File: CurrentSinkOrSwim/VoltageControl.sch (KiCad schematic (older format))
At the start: 7 parts, among them U201 LMV358

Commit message: cambiando potenciómetro y divisores de tension
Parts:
- R201: value R -> 27,8K
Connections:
- net 2.7V: now also R201.1; no longer RV201.2
- net Current_Sink-: now also RV201.3; no longer R201.2
- new net: R201.2, RV201.2, U201.3 (+)
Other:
- note added: "0-20V"
- note added: "0-2V"
- note added: "Como queremos que como máximo tengamos 20V (porque con 1A de mínimo\nen la fuente de corriente, con 20V de batería en el MOSFET se disipan 20W), el\ndivisor de tensión tendrá que dar en el + 2V."
- note added: "Con este potenciómetro controlar el máximo voltaje de la batería.\nEl valor que pongas en el + lo multiplicas por 10 y ese es el valor máximo"
- note added: "Si la batería supera los 20V, el MOSFET tendrá que dejar de funcionar y la batería se conecta directamente a tierra"
- moved on the sheet: R201
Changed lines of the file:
@@
 Sheet 2 4
 Title ""
-Date "7 sep 2015"
+Date "19 sep 2015"
 Rev ""
 Comp ""
@@
 L R R201
 U 1 1 55E5F049
-P 3600 5200
-F 0 "R201" V 3680 5200 40  0000 C CNN
-F 1 "R" V 3607 5201 40  0000 C CNN
-F 2 "~" V 3530 5200 30  0000 C CNN
-F 3 "~" H 3600 5200 30  0000 C CNN
-	1    3600 5200
+P 3900 3650
+F 0 "R201" V 3980 3650 40  0000 C CNN
+F 1 "27,8K" V 3907 3651 40  0000 C CNN
+F 2 "~" V 3830 3650 30  0000 C CNN
+F 3 "~" H 3900 3650 30  0000 C CNN
+	1    3900 3650
 	1    0    0    -1
 $EndComp
@@
 	5850 4100 5850 4250
 Wire Wire Line
-	3600 4600 3600 4950
-Wire Wire Line
 	5450 3800 5200 3800
 Wire Wire Line
@@
 	5450 3600 4800 3600
 Wire Wire Line
-	4800 3600 4800 4750
-Wire Wire Line
-	4800 4750 3600 4750
-Connection ~ 3600 4750
-Wire Wire Line
-	3600 5450 3600 5550
+	3600 4600 3600 5550
 Wire Wire Line
 	3600 5550 9200 5550
-Wire Wire Line
-	3900 4350 3750 4350
 Wire Wire Line
 	5850 2950 5850 3300
@@
 Wire Wire Line
 	3250 1900 3900 1900
-Wire Wire Line
-	3900 1900 3900 4350
-Connection ~ 3900 2950
 Wire Wire Line
 	6450 3700 6800 3700
@@
 Text HLabel 9200 3700 2    60   Output ~ 0
 Vcontrol
+Text Notes 750  1000 0    60   ~ 0
+Con este potenciómetro controlar el máximo voltaje de la batería.\nEl valor que pongas en el + lo multiplicas por 10 y ese es el valor máximo
+Text Notes 750  1200 0    60   ~ 0
+Como queremos que como máximo tengamos 20V (porque con 1A de mínimo\nen la fuente de corriente, con 20V de batería en el MOSFET se disipan 20W), el\ndivisor de tensión tendrá que dar en el + 2V.
+Text Notes 750  1500 0    60   ~ 0
+Si la batería supera los 20V, el MOSFET tendrá que dejar de funcionar y la batería se conecta directamente a tierra
+Wire Wire Line
+	3900 1900 3900 3400
+Wire Wire Line
+	3750 4350 4800 4350
+Wire Wire Line
+	3900 3900 3900 4350
+Connection ~ 3900 2950
+Wire Wire Line
+	4800 4350 4800 3600
+Connection ~ 3900 4350
+Text Notes 4250 4350 0    60   ~ 0
+0-2V
+Text Notes 6700 4450 0    60   ~ 0
+0-2V
+Text Notes 8800 3850 0    60   ~ 0
+0-20V
 $EndSCHEMATC

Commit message: placing components in the PCB
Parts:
- renumbered 1N4148WT-7 to D201
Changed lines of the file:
@@
 $EndComp
 $Comp
-L GND #PWR03
+L GND #PWR202
 U 1 1 55E5F04F
 P 5850 4250
-F 0 "#PWR03" H 5850 4250 30  0001 C CNN
+F 0 "#PWR202" H 5850 4250 30  0001 C CNN
 F 1 "GND" H 5850 4180 30  0001 C CNN
 F 2 "~" H 5850 4250 60  0000 C CNN
@@
 $EndComp
 $Comp
-L GND #PWR04
+L GND #PWR201
 U 1 1 55E5F061
 P 5350 3450
-F 0 "#PWR04" H 5350 3450 30  0001 C CNN
+F 0 "#PWR201" H 5350 3450 30  0001 C CNN
 F 1 "GND" H 5350 3380 30  0001 C CNN
 F 2 "~" H 5350 3450 60  0000 C CNN
@@
 	6450 3700 6800 3700
 $Comp
-L DIODE 1N4148WT-7
+L DIODE D201
 U 1 1 55E5F084
 P 7000 3700
-F 0 "1N4148WT-7" H 7000 3800 40  0000 C CNN
+F 0 "D201" H 7000 3800 40  0000 C CNN
 F 1 "DIODE" H 7000 3600 40  0000 C CNN
 F 2 "~" H 7000 3700 60  0000 C CNN

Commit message: Layout session 2
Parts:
- removed C201: C, ~, symbol C
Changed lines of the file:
@@
 Sheet 2 4
 Title ""
-Date "19 sep 2015"
+Date "24 sep 2015"
 Rev ""
 Comp ""
@@
 $EndComp
 $Comp
-L GND #PWR202
+L GND #PWR03
 U 1 1 55E5F04F
 P 5850 4250
-F 0 "#PWR202" H 5850 4250 30  0001 C CNN
+F 0 "#PWR03" H 5850 4250 30  0001 C CNN
 F 1 "GND" H 5850 4180 30  0001 C CNN
 F 2 "~" H 5850 4250 60  0000 C CNN
@@
 	1    3600 4350
 	0    1    1    0
-$EndComp
-$Comp
-L C C201
-U 1 1 55E5F05B
-P 5350 3200
-F 0 "C201" H 5350 3300 40  0000 L CNN
-F 1 "C" H 5356 3115 40  0000 L CNN
-F 2 "~" H 5388 3050 30  0000 C CNN
-F 3 "~" H 5350 3200 60  0000 C CNN
-	1    5350 3200
-	1    0    0    -1
-$EndComp
-$Comp
-L GND #PWR201
-U 1 1 55E5F061
-P 5350 3450
-F 0 "#PWR201" H 5350 3450 30  0001 C CNN
-F 1 "GND" H 5350 3380 30  0001 C CNN
-F 2 "~" H 5350 3450 60  0000 C CNN
-F 3 "~" H 5350 3450 60  0000 C CNN
-	1    5350 3450
-	1    0    0    -1
 $EndComp
 Wire Wire Line
@@
 	3900 2950 5850 2950
 Wire Wire Line
-	5350 3000 5350 2950
-Connection ~ 5350 2950
-Wire Wire Line
-	5350 3400 5350 3450
-Wire Wire Line
 	5200 4450 8600 4450

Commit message: Actualizando información de los componentes y creando el BOM
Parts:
- D201: MFG Name (none) -> 1N4148WT-7; MFG Part Number 1N4148WT-7 -> (none)
- RV201: MFG Name (none) -> ALPS 29 0001 POTENCIOMETRO
- U201: MFG Name (none) -> LMV358ID; MFG Part Number LMV358ID -> (none)
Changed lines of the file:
@@
 Sheet 2 4
 Title ""
-Date "24 sep 2015"
+Date "1 oct 2015"
 Rev ""
 Comp ""
@@
 F 2 "" H 5950 3700 60  0000 C CNN
 F 3 "" H 5950 3700 60  0000 C CNN
-F 4 " LMV358ID" H 5950 3700 60  0001 C CNN "MFG Part Number"
+F 4 " LMV358ID" H 5950 3700 60  0001 C CNN "MFG Name"
 F 5 "http://www.farnell.com/datasheets/1862405.pdf" H 5950 3700 60  0001 C CNN "Distributor Part Number 1"
 	1    5950 3700
@@
 F 2 "~" H 3600 4350 60  0000 C CNN
 F 3 "~" H 3600 4350 60  0000 C CNN
+F 4 "ALPS 29 0001  POTENCIOMETRO" H 3600 4350 60  0001 C CNN "MFG Name"
 	1    3600 4350
 	0    1    1    0
@@
 F 2 "~" H 7000 3700 60  0000 C CNN
 F 3 "http://www.farnell.com/datasheets/1915502.pdf" H 7000 3700 60  0001 C CNN
-F 4 "1N4148WT-7" H 7000 3700 60  0001 C CNN "MFG Part Number"
+F 4 "1N4148WT-7" H 7000 3700 60  0001 C CNN "MFG Name"
 	1    7000 3700
 	-1   0    0    1

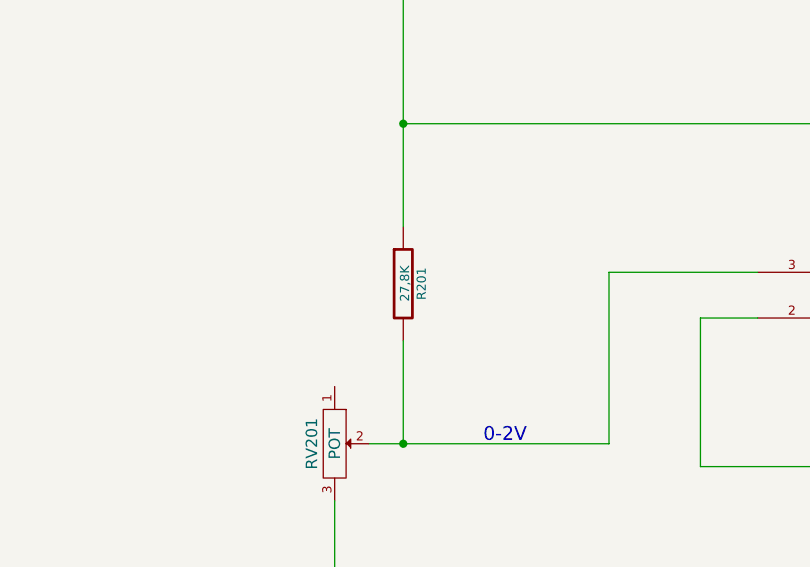
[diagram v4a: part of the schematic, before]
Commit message: Haciendo algunos cambios porque he tenido que cambiar de componentes y algún valor estaba mal
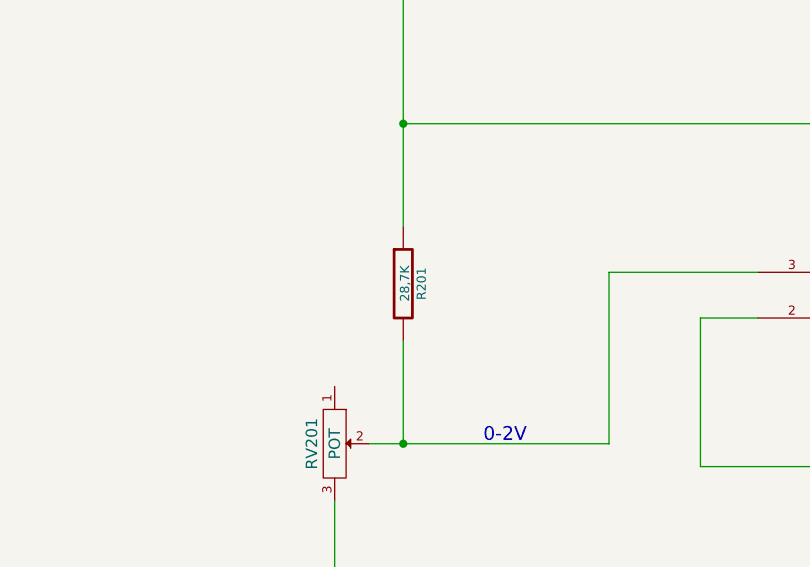
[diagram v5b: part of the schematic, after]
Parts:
- R201: value 27,8K -> 28,7K
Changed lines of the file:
@@
 Sheet 2 4
 Title ""
-Date "1 oct 2015"
+Date "5 oct 2015"
 Rev ""
 Comp ""
@@
 P 3900 3650
 F 0 "R201" V 3980 3650 40  0000 C CNN
-F 1 "27,8K" V 3907 3651 40  0000 C CNN
+F 1 "28,7K" V 3907 3651 40  0000 C CNN
 F 2 "~" V 3830 3650 30  0000 C CNN
 F 3 "~" H 3900 3650 30  0000 C CNN
